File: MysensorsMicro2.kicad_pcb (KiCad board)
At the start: 2 copper layers, 18.7 x 30.5 mm, 29 parts, among them P1 Debug, P2 MYSX_1.2, P3 Antenna, U1 ATSAMD21E, U2 AP1117D33, U3 NRF24L01, U4 RFM69HW, U5 ATSHA204A, U6 AT25DF512C, U7 Si7021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

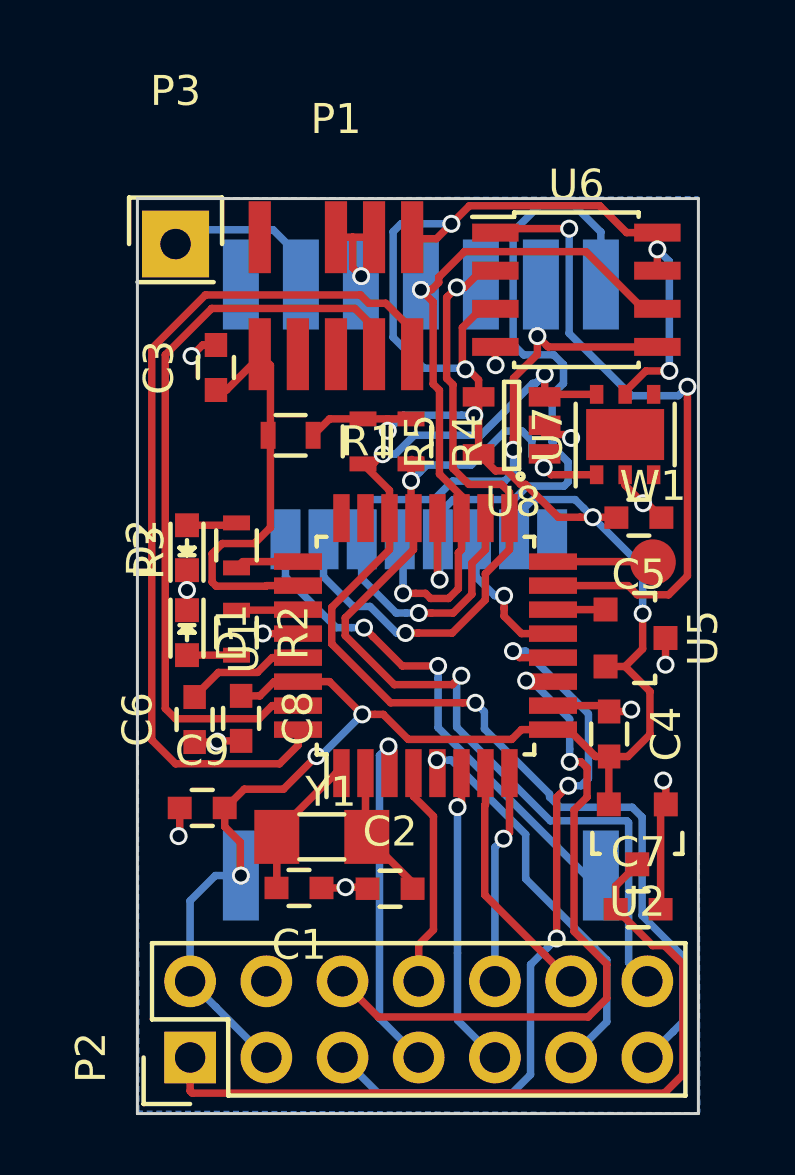
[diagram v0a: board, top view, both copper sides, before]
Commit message: Added testpads to reset signal + gnd
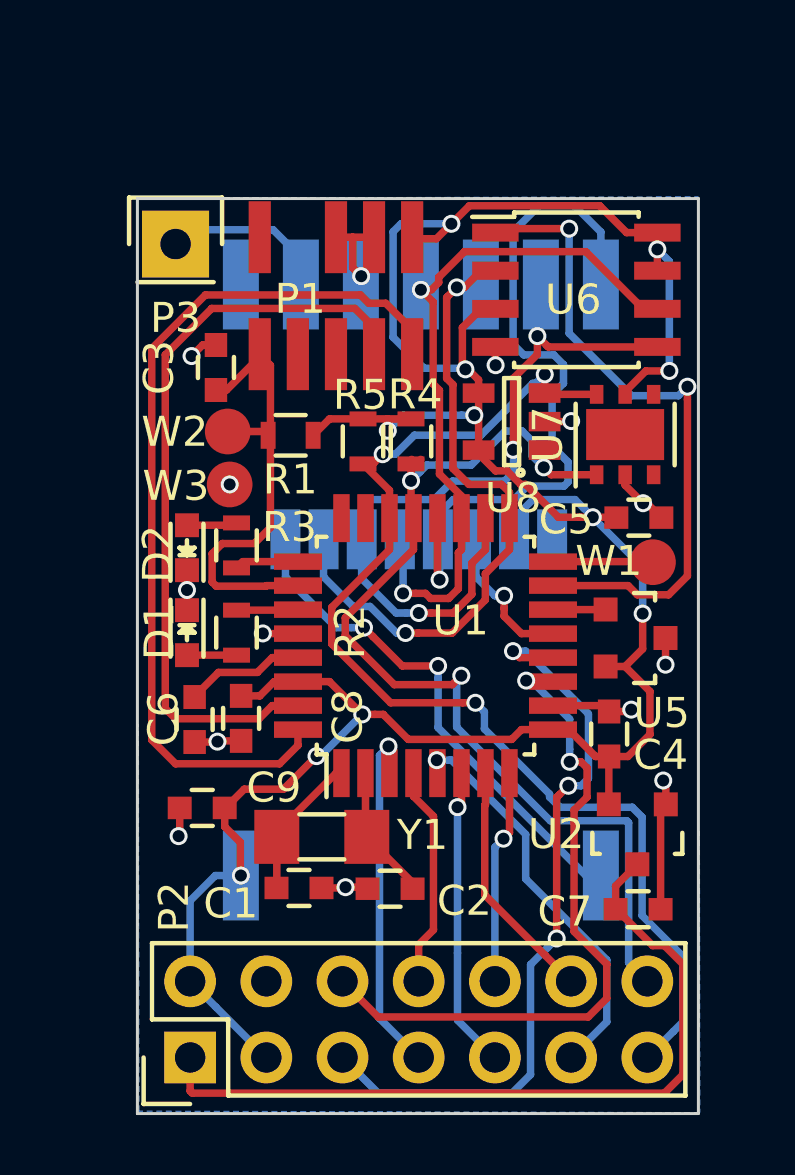
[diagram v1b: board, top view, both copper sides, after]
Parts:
- added W2: RESET, Measurement_Points:Measurement_Point_Round-SMD-Pad_Small, F.Cu at (92.0, 89.9)
- added W3: GND, Measurement_Points:Measurement_Point_Round-SMD-Pad_Small, F.Cu at (92.1, 91.6)
- C1, C2, C4, C5, C6, C8, C9: value C -> 100nF
- R2, R3: value R -> 220R
- W1: value TEST_1P -> BOOTL
- moved U8 0.13 mm to (101.5, 89.5)
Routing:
- net /RESET: track 14.0 -> 15.6 mm
- net GND: track 22.3 -> 22.2 mm, vias 13 -> 14
